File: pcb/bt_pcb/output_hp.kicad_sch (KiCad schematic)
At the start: 10 parts, among them IC3 TPA6130A2RTJR, J13 AudioJack3

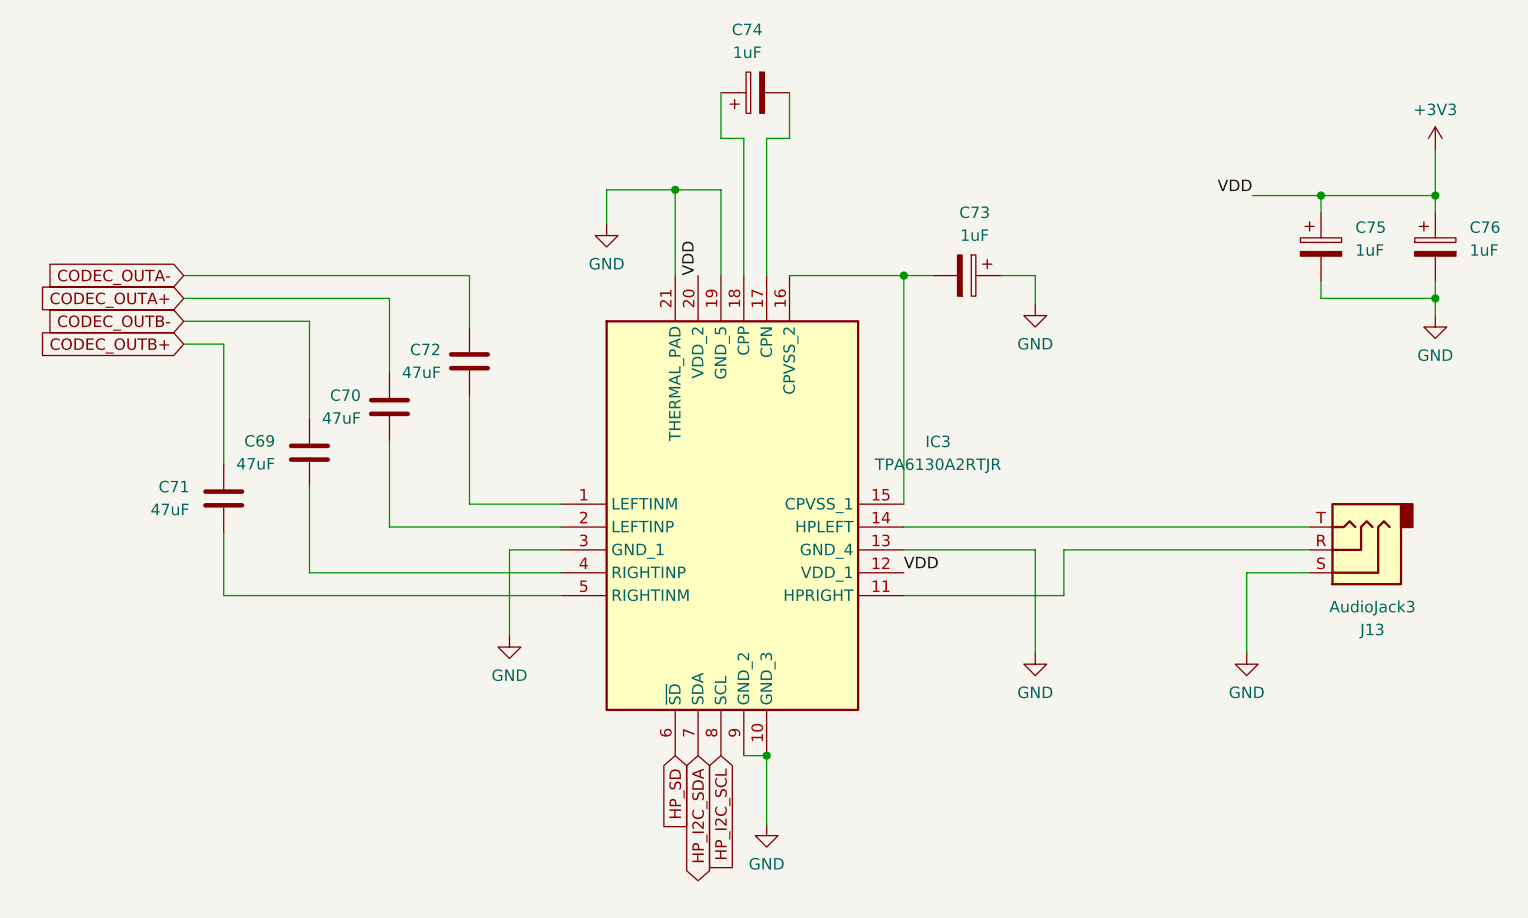
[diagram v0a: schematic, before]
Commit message: ditching power pcb, new codec
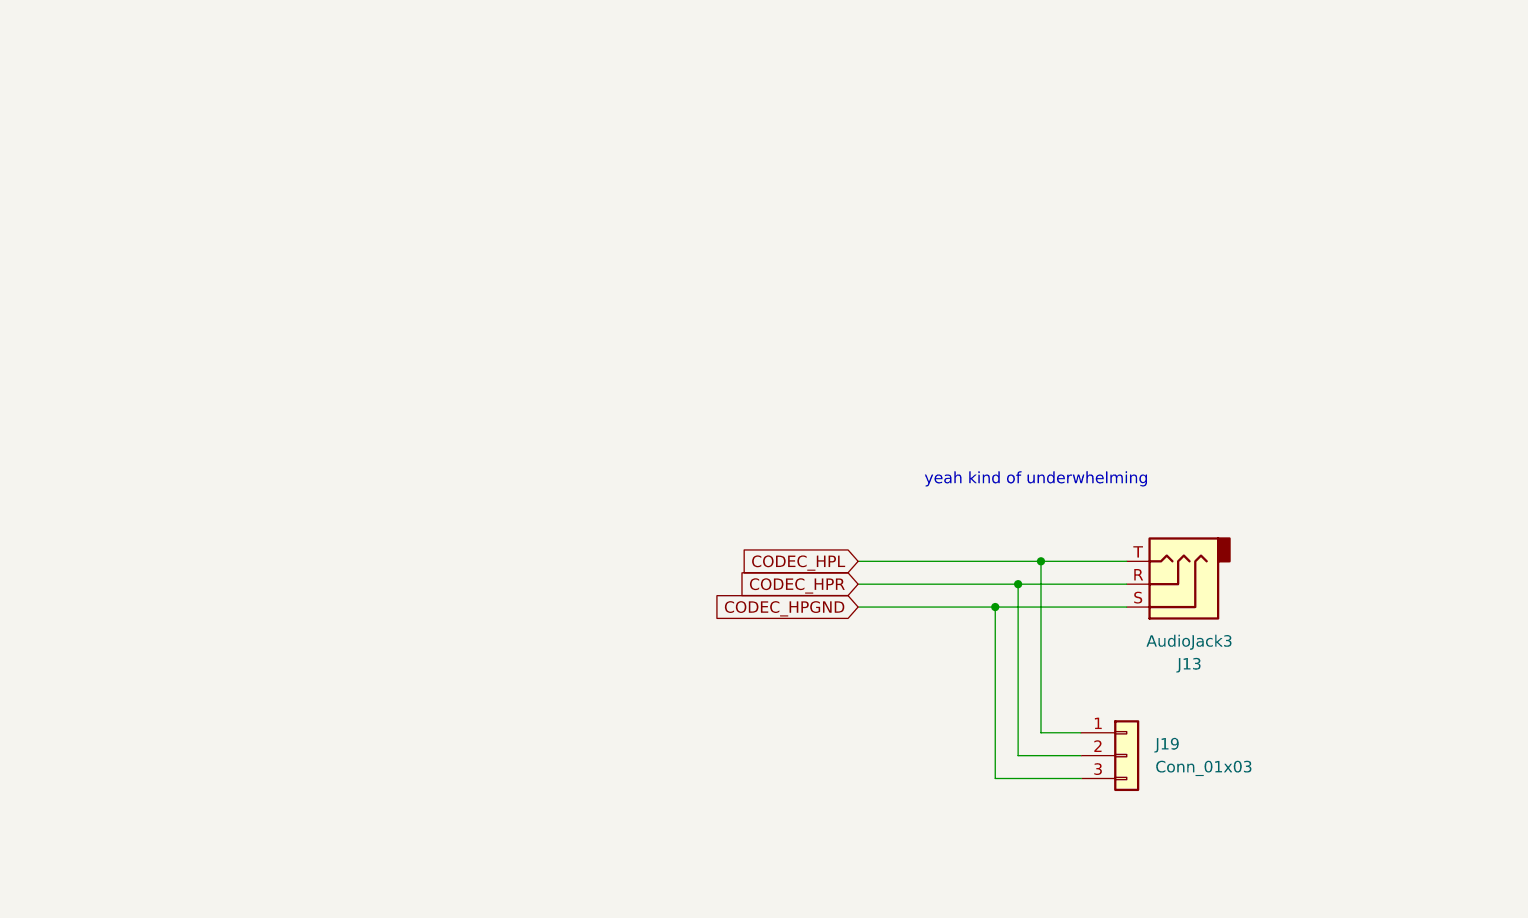
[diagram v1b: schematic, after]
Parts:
- removed C69, C70, C71, C72: 47uF, symbol Device:C
- removed C73, C74, C75, C76: 1uF, symbol Device:C_Polarized
- removed IC3: TPA6130A2RTJR, library:QFN50P400X400X80-21N-D, symbol library:TPA6130A2RTJR
- added J19: Conn_01x03, symbol Connector_Generic:Conn_01x03
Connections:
- net CODEC_HPR: now reaches J13.R
- net CODEC_HPR: now also J19.2 (Pin_2)
- net CODEC_HPL: now reaches J13.T
- net CODEC_HPL: now also J19.1 (Pin_1)
- net GND renamed CODEC_HPGND
- net CODEC_HPGND: now also J19.3 (Pin_3)
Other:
- note added: "yeah kind of underwhelming"
- moved on the sheet: J13

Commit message: solving some erc warnings and errors
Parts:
- renumbered J19 to J10, J13 to J11
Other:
- moved on the sheet: J10, J11
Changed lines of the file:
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@@
 	(text "yeah kind of underwhelming"
 		(exclude_from_sim no)
-		(at 168.402 88.138 0)
+		(at 168.91 88.9 0)
 		(effects
 			(font
@@
 	)
 	(junction
-		(at 163.83 102.235)
+		(at 163.83 102.87)
 		(diameter 0)
 		(color 0 0 0 0)
 	)
 	(junction
-		(at 166.37 99.695)
+		(at 166.37 100.33)
 		(diameter 0)
 		(color 0 0 0 0)
 	)
 	(junction
-		(at 168.91 97.155)
+		(at 168.91 97.79)
 		(diameter 0)
 		(color 0 0 0 0)
@@
 	(wire
 		(pts
-			(xy 173.355 116.205) (xy 168.91 116.205)
-		)
-		(stroke
-			(width 0)
-			(type default)
-		)
-	)
-	(wire
-		(pts
-			(xy 173.355 118.745) (xy 166.37 118.745)
-		)
-		(stroke
-			(width 0)
-			(type default)
-		)
-	)
-	(wire
-		(pts
-			(xy 173.355 121.285) (xy 163.83 121.285)
-		)
-		(stroke
-			(width 0)
-			(type default)
-		)
-	)
-	(wire
-		(pts
-			(xy 168.91 116.205) (xy 168.91 97.155)
-		)
-		(stroke
-			(width 0)
-			(type default)
-		)
-	)
-	(wire
-		(pts
-			(xy 163.83 102.235) (xy 163.83 121.285)
-		)
-		(stroke
-			(width 0)
-			(type default)
-		)
-	)
-	(wire
-		(pts
-			(xy 166.37 118.745) (xy 166.37 99.695)
-		)
-		(stroke
-			(width 0)
-			(type default)
-		)
-	)
-	(wire
-		(pts
-			(xy 166.37 99.695) (xy 178.435 99.695)
-		)
-		(stroke
-			(width 0)
-			(type default)
-		)
-	)
-	(wire
-		(pts
-			(xy 148.59 102.235) (xy 163.83 102.235)
-		)
-		(stroke
-			(width 0)
-			(type default)
-		)
-	)
-	(wire
-		(pts
-			(xy 168.91 97.155) (xy 178.435 97.155)
-		)
-		(stroke
-			(width 0)
-			(type default)
-		)
-	)
-	(wire
-		(pts
-			(xy 148.59 97.155) (xy 168.91 97.155)
-		)
-		(stroke
-			(width 0)
-			(type default)
-		)
-	)
-	(wire
-		(pts
-			(xy 148.59 99.695) (xy 166.37 99.695)
-		)
-		(stroke
-			(width 0)
-			(type default)
-		)
-	)
-	(wire
-		(pts
-			(xy 163.83 102.235) (xy 178.435 102.235)
+			(xy 173.99 116.84) (xy 168.91 116.84)
+		)
+		(stroke
+			(width 0)
+			(type default)
+		)
+	)
+	(wire
+		(pts
+			(xy 173.99 119.38) (xy 166.37 119.38)
+		)
+		(stroke
+			(width 0)
+			(type default)
+		)
+	)
+	(wire
+		(pts
+			(xy 173.99 121.92) (xy 163.83 121.92)
+		)
+		(stroke
+			(width 0)
+			(type default)
+		)
+	)
+	(wire
+		(pts
+			(xy 168.91 116.84) (xy 168.91 97.79)
+		)
+		(stroke
+			(width 0)
+			(type default)
+		)
+	)
+	(wire
+		(pts
+			(xy 163.83 102.87) (xy 163.83 121.92)
+		)
+		(stroke
+			(width 0)
+			(type default)
+		)
+	)
+	(wire
+		(pts
+			(xy 166.37 119.38) (xy 166.37 100.33)
+		)
+		(stroke
+			(width 0)
+			(type default)
+		)
+	)
+	(wire
+		(pts
+			(xy 166.37 100.33) (xy 179.07 100.33)
+		)
+		(stroke
+			(width 0)
+			(type default)
+		)
+	)
+	(wire
+		(pts
+			(xy 148.59 102.87) (xy 163.83 102.87)
+		)
+		(stroke
+			(width 0)
+			(type default)
+		)
+	)
+	(wire
+		(pts
+			(xy 168.91 97.79) (xy 179.07 97.79)
+		)
+		(stroke
+			(width 0)
+			(type default)
+		)
+	)
+	(wire
+		(pts
+			(xy 148.59 97.79) (xy 168.91 97.79)
+		)
+		(stroke
+			(width 0)
+			(type default)
+		)
+	)
+	(wire
+		(pts
+			(xy 148.59 100.33) (xy 166.37 100.33)
+		)
+		(stroke
+			(width 0)
+			(type default)
+		)
+	)
+	(wire
+		(pts
+			(xy 163.83 102.87) (xy 179.07 102.87)
 		)
 		(stroke
@@
 	(global_label "CODEC_HPGND"
 		(shape input)
-		(at 148.59 102.235 180)
+		(at 148.59 102.87 180)
 		(fields_autoplaced yes)
 		(effects
@@
 		)
 		(property "Intersheetrefs" "${INTERSHEET_REFS}"
-			(at 131.8767 102.235 0)
+			(at 131.8767 102.87 0)
 			(effects
 				(font
@@
 	(global_label "CODEC_HPL"
 		(shape input)
-		(at 148.59 97.155 180)
+		(at 148.59 97.79 180)
 		(fields_autoplaced yes)
 		(effects
@@
 		)
 		(property "Intersheetrefs" "${INTERSHEET_REFS}"
-			(at 134.7191 97.155 0)
+			(at 134.7191 97.79 0)
 			(effects
 				(font
@@
 	(global_label "CODEC_HPR"
 		(shape input)
-		(at 148.59 99.695 180)
+		(at 148.59 100.33 180)
 		(fields_autoplaced yes)
 		(effects
@@
 		)
 		(property "Intersheetrefs" "${INTERSHEET_REFS}"
-			(at 134.4772 99.695 0)
+			(at 134.4772 100.33 0)
 			(effects
 				(font
@@
 	(symbol
 		(lib_id "Connector_Audio:AudioJack3")
-		(at 183.515 99.695 180)
+		(at 184.15 100.33 180)
 		(unit 1)
 		(exclude_from_sim no)
@@
 		(on_board yes)
 		(dnp no)
-		(property "Reference" "J13"
-			(at 185.42 108.585 0)
+		(property "Reference" "J11"
+			(at 186.055 109.22 0)
 			(effects
 				(font
@@
 		)
 		(property "Value" "AudioJack3"
-			(at 185.42 106.045 0)
+			(at 186.055 106.68 0)
 			(effects
 				(font
@@
 		)
 		(property "Footprint" ""
-			(at 183.515 99.695 0)
+			(at 184.15 100.33 0)
 			(effects
 				(font
@@
 		)
 		(property "Datasheet" "~"
-			(at 183.515 99.695 0)
+			(at 184.15 100.33 0)
 			(effects
 				(font
@@
 		)
 		(property "Description" ""
-			(at 183.515 99.695 0)
+			(at 184.15 100.33 0)
 			(effects
 				(font
@@
 			(project "bt_pcb"
 				(path "/eb787481-08cd-41a4-a128-173fa6227c32/4ada0139-8712-47ce-9d4c-ab8fef312f7b/dc98d12f-0323-4fbb-9954-b3059d58104c"
-					(reference "J13")
+					(reference "J11")
 					(unit 1)
 				)
@@
 	(symbol
 		(lib_id "Connector_Generic:Conn_01x03")
-		(at 178.435 118.745 0)
+		(at 179.07 119.38 0)
 		(unit 1)
 		(exclude_from_sim no)
@@
 		(dnp no)
 		(fields_autoplaced yes)
-		(property "Reference" "J19"
-			(at 181.61 117.4749 0)
+		(property "Reference" "J10"
+			(at 182.245 118.1099 0)
 			(effects
 				(font
@@
 		)
 		(property "Value" "Conn_01x03"
-			(at 181.61 120.0149 0)
+			(at 182.245 120.6499 0)
 			(effects
 				(font
@@
 		)
 		(property "Footprint" ""
-			(at 178.435 118.745 0)
+			(at 179.07 119.38 0)
 			(effects
 				(font
@@
 		)
 		(property "Datasheet" "~"
-			(at 178.435 118.745 0)
+			(at 179.07 119.38 0)
 			(effects
 				(font
@@
 		)
 		(property "Description" "Generic connector, single row, 01x03, script generated (kicad-library-utils/schlib/autogen/connector/)"
-			(at 178.435 118.745 0)
+			(at 179.07 119.38 0)
 			(effects
 				(font
@@
 			(project ""
 				(path "/eb787481-08cd-41a4-a128-173fa6227c32/4ada0139-8712-47ce-9d4c-ab8fef312f7b/dc98d12f-0323-4fbb-9954-b3059d58104c"
-					(reference "J19")
+					(reference "J10")
 					(unit 1)
 				)
